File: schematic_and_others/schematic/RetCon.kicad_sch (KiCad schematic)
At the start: 32 parts, among them J5 programming port, J6 USB_B_Micro, SW1 SW_SPDT, SW2 Home, SW3 BumperR, SW4 Select, SW5 BumperL, SW6 TriggerR, SW7 TriggerL, U1 ATmega1284P, U2 L7805, U3 WG12864B-STBL, U4 LF33_TO252, U5 SN74LS07, U6 SD, Y1 16Mhz

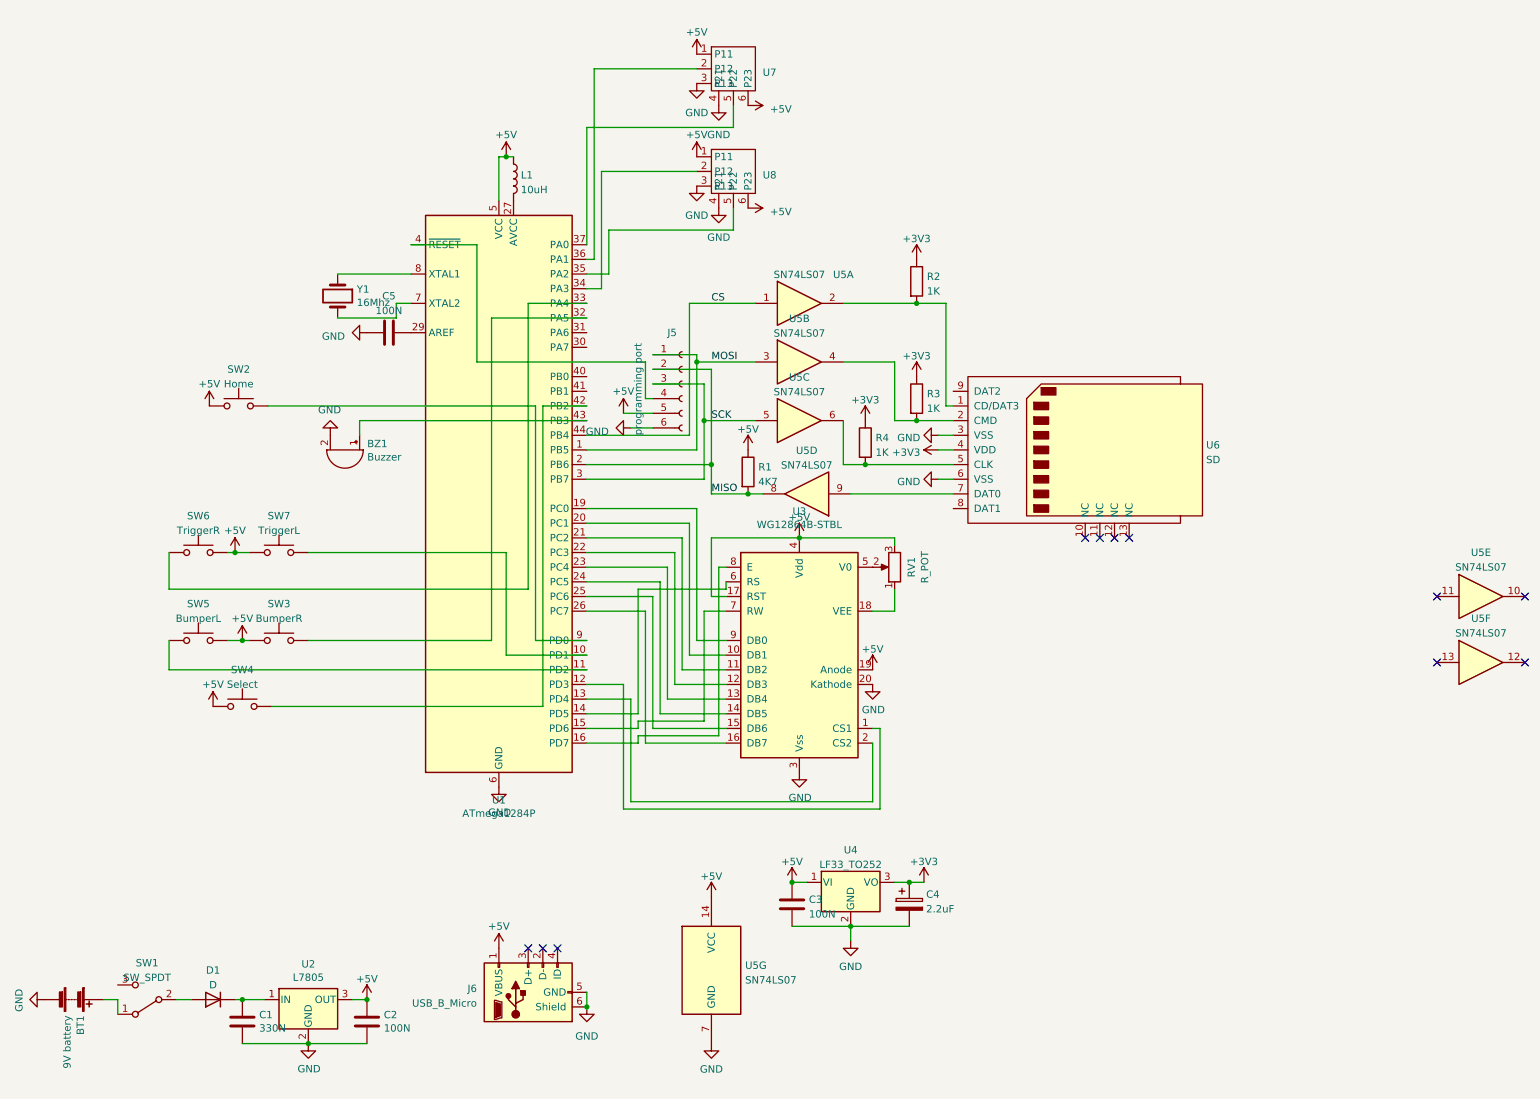
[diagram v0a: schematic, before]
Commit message: Better schematic
- fixed mistake of connecting buttons to +5V
- clearer schematic
- PCB to update
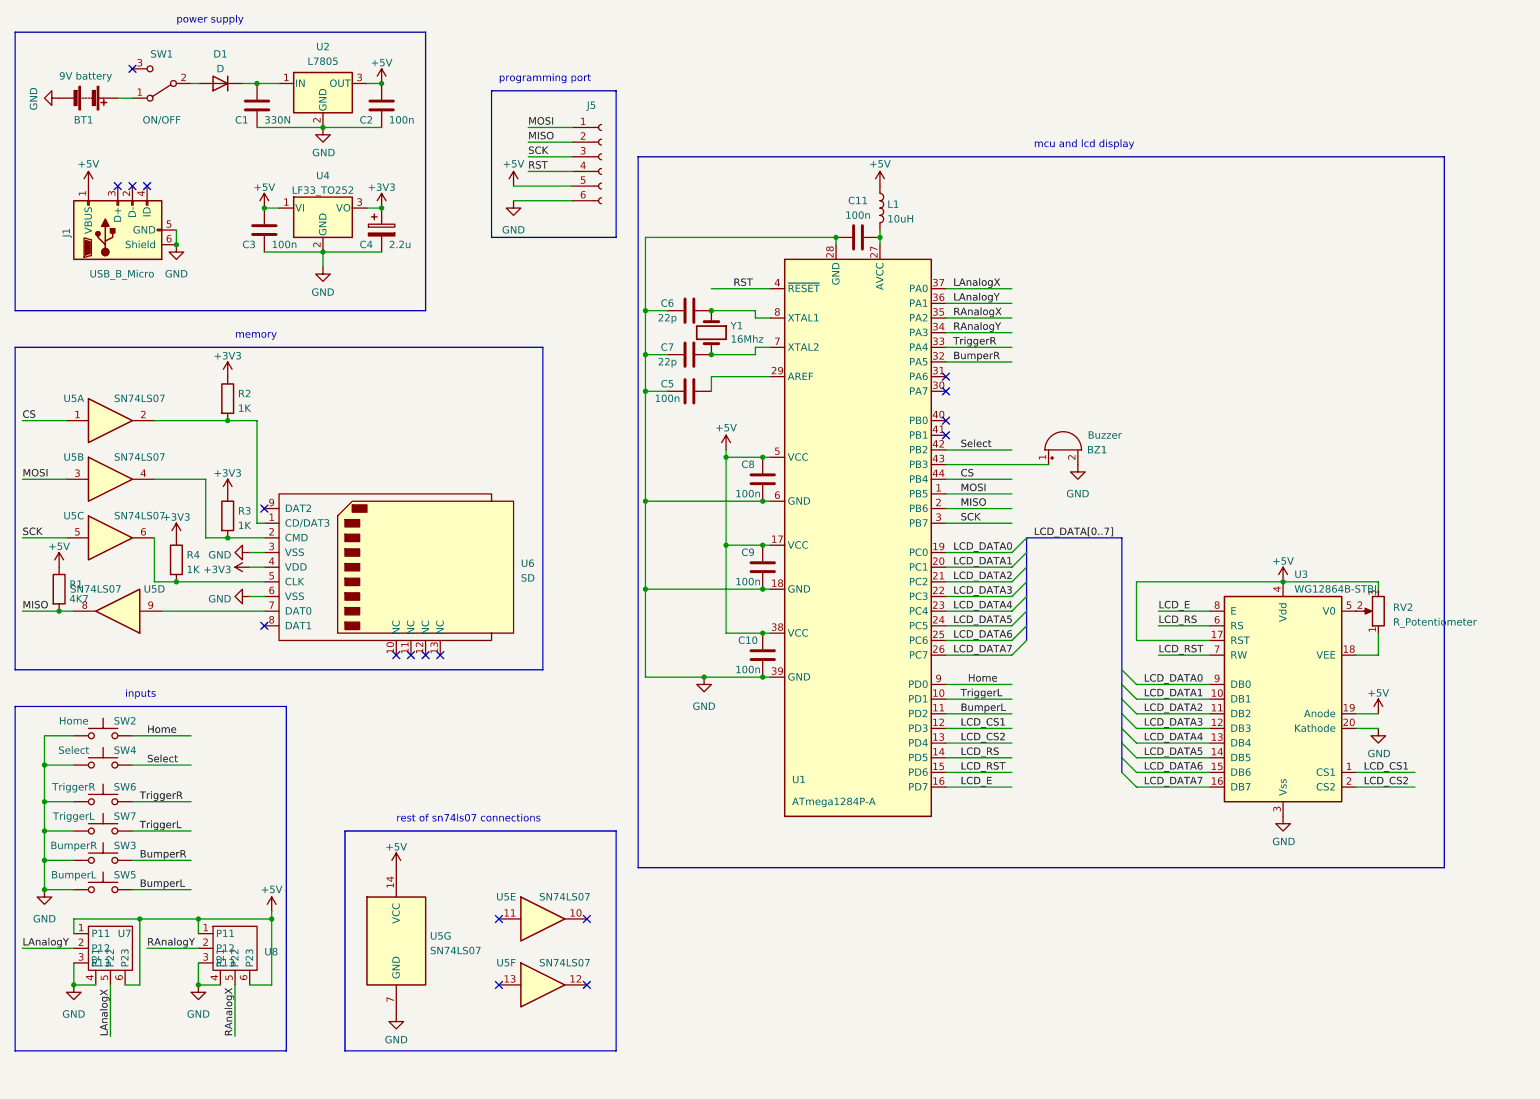
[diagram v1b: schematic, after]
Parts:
- removed J6: USB_B_Micro, USB:USBMicro-SMD, symbol Connector:USB_B_Micro
- removed RV1: R_POT, Blue:potentiometer10K, symbol Device:R_POT
- removed U1: ATmega1284P, Package_QFP:TQFP-44_10x10mm_P0.8mm, symbol MCU_Microchip_ATmega:ATmega32A-AU
- removed U2: L7805, Package_TO_SOT_SMD:TO-263-2, symbol Regulator_Linear:L7805
- removed U3: WG12864B-STBL, Blue:WG12864BL, symbol schemat_dip40-rescue:WG12864B-STBL
- removed U6: SD, Connector_Card:SD_Kyocera_145638009511859+, symbol sd:SD
- removed U7, U8: ~, joystick:joystickTHT, symbol joystick:joystickTHT
- added C10, C11, C8, C9: 100n, Capacitor_SMD:C_0805_2012Metric, symbol Device:C
- added C6, C7: 22p, Capacitor_SMD:C_0805_2012Metric, symbol Device:C
- added J1: USB_B_Micro, USB:USBMicro-SMD, symbol RetCon:USB_B_Micro
- added RV2: R_Potentiometer, Blue:potentiometer10K, symbol Device:R_Potentiometer
- added U1: ATmega1284P-A, Package_QFP:TQFP-44_10x10mm_P0.8mm, symbol RetCon:ATmega1284P-A
- added U2: L7805, Package_TO_SOT_SMD:TO-263-2, symbol RetCon:L7805
- added U3: WG12864B-STBL, Blue:WG12864BL, symbol RetCon:WG12864B-STBL
- added U6: SD, Connector_Card:SD_Kyocera_145638009511859+, symbol RetCon:SD
- added U7, U8: ~, joystick:joystickTHT, symbol RetCon:joystickTHT
- C2, C3, C5: value 100N -> 100n
- C4: value 2.2uF -> 2.2u
- J5: value programming port -> ~
- SW1: value SW_SPDT -> ON/OFF
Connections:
- net +3V3: now also U6.4 (VDD)
- net +5V: now also C10.2, C8.2, C9.2, J1.1 (VBUS), RV2.3, U1.17 (VCC), U1.38 (VCC), U1.5 (VCC), U2.3 (OUT), U3.17 (RST), U3.19 (Anode), U3.4 (Vdd), U7.1 (P11), U7.6 (P23), U8.1 (P11), U8.6 (P23); no longer SW2.1, SW3.1, SW4.1, SW5.2, SW6.2, SW7.1
- net CS: now also U1.44 (PB4)
- net GND: now also C5.1, SW2.1, SW3.1, SW4.1, SW5.1, SW6.1, SW7.1, C10.1, C11.1, C6.1, C7.1, C8.1, C9.1, J1.5 (GND), J1.6 (Shield), U1.18 (GND), U1.28 (GND), U1.39 (GND), U1.6 (GND), U2.2 (GND), U3.20 (Kathode), U3.3 (Vss), U6.3 (VSS), U6.6 (VSS), U7.3 (P13), U7.4 (P21), U8.3 (P13), U8.4 (P21); no longer C5.2
- net MISO: now also U1.2 (PB6); no longer J5.3 (Pin_3), U5.5
- net MOSI: now also U1.1 (PB5)
- net TriggerL: now reaches SW7.2
- net TriggerL: now also U1.10 (PD1)
- net at L1.2: now also C11.2, U1.27 (AVCC)
- net BumperR: now reaches SW3.2
- net BumperR: now also U1.32 (PA5)
- net RST: now reaches J5.4 (Pin_4)
- net RST: now also U1.4 (~{RESET})
- net Select: now reaches SW4.2
- net Select: now also U1.42 (PB2)
- net at BZ1.1 (-): now also U1.43 (PB3)
- net at Y1.2: now also C7.2, U1.7 (XTAL2)
- net at Y1.1: now also C6.2, U1.8 (XTAL1)
- net Home: now reaches SW2.2
- net Home: now also U1.9 (PD0)
- net at C1.1, D1.1 (K): now also U2.1 (IN)
- net at R4.2, U5.6: now also U6.5 (CLK)
- net at R3.2, U5.4: now also U6.2 (CMD)
- net at U5.9: now also U6.7 (DAT0)
- net at R2.2, U5.2: now also U6.1 (CD/DAT3)
- new net: RV2.1, U3.18 (VEE)
- new net: RV2.2, U3.5 (V0)
- new net: C5.2, U1.29 (AREF)
- new net BumperL: SW5.2, U1.11 (PD2)
- new net LAnalogX: U1.37 (PA0), U7.5 (P22)
- new net LAnalogY: U1.36 (PA1), U7.2 (P12)
- new net LCD_CS1: U1.12 (PD3), U3.1 (CS1)
- new net LCD_CS2: U1.13 (PD4), U3.2 (CS2)
- new net LCD_DATA0: U1.19 (PC0), U3.9 (DB0)
- new net LCD_DATA1: U1.20 (PC1), U3.10 (DB1)
- new net LCD_DATA2: U1.21 (PC2), U3.11 (DB2)
- new net LCD_DATA3: U1.22 (PC3), U3.12 (DB3)
- new net LCD_DATA4: U1.23 (PC4), U3.13 (DB4)
- new net LCD_DATA5: U1.24 (PC5), U3.14 (DB5)
- new net LCD_DATA6: U1.25 (PC6), U3.15 (DB6)
- new net LCD_DATA7: U1.26 (PC7), U3.16 (DB7)
- new net LCD_E: U1.16 (PD7), U3.8 (E)
- new net LCD_RS: U1.14 (PD5), U3.6 (RS)
- new net LCD_RST: U1.15 (PD6), U3.7 (RW)
- new net RAnalogX: U1.35 (PA2), U8.5 (P22)
- new net RAnalogY: U1.34 (PA3), U8.2 (P12)
- new net SCK: J5.3 (Pin_3), U1.3 (PB7), U5.5
- new net TriggerR: SW6.2, U1.33 (PA4)
- no-connect marks 11 -> 18
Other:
- note added: "inputs"
- note added: "mcu and lcd display"
- note added: "memory"
- note added: "power supply"
- note added: "programming port"
- note added: "rest of sn74ls07 connections"
- moved on the sheet: BT1, BZ1, C1, C2, C3, C4, C5, D1, J5, L1, R1, R2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

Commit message: Board update
- capacitors placed and connected
- buttons connected to ground
- need to update buttons and display footprints
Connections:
- net BumperR: now also SW3.1; no longer SW3.2
- net GND: now also SW3.2, SW6.2; no longer SW3.1, SW6.1
- net TriggerR: now also SW6.1; no longer SW6.2
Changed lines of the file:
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@@
     )
   )
-  (symbol (lib_id "Switch:SW_Push") (at 30.48 158.75 0) (unit 1)
+  (symbol (lib_id "Switch:SW_Push") (at 30.48 158.75 0) (mirror y) (unit 1)
     (in_bom yes) (on_board yes) (dnp no)
     (property "Reference" "SW3" (at 34.29 156.21 0)
@@
     )
   )
-  (symbol (lib_id "Switch:SW_Push") (at 30.48 148.59 0) (unit 1)
+  (symbol (lib_id "Switch:SW_Push") (at 30.48 148.59 0) (mirror y) (unit 1)
     (in_bom yes) (on_board yes) (dnp no)
     (property "Reference" "SW6" (at 34.29 146.05 0)

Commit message: Board sent to manufacturer
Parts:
- renumbered RV2 to RV1
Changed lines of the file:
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@@
   (symbol (lib_id "Device:R_Potentiometer") (at 251.46 115.57 180) (unit 1)
     (in_bom yes) (on_board yes) (dnp no) (fields_autoplaced)
-    (property "Reference" "RV2" (at 254 114.935 0)
+    (property "Reference" "RV1" (at 254 114.935 0)
       (effects (font (size 1.27 1.27)) (justify right))
     )
@@
       (project "RetCon"
         (path "/275aa44a-b61f-489f-9e2a-819a0fe0d1eb"
-          (reference "RV2") (unit 1)
+          (reference "RV1") (unit 1)
         )
       )
